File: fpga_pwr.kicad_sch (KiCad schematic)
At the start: 29 parts, among them Q1 BC817, U8 LFE5U-25F-8MG285C

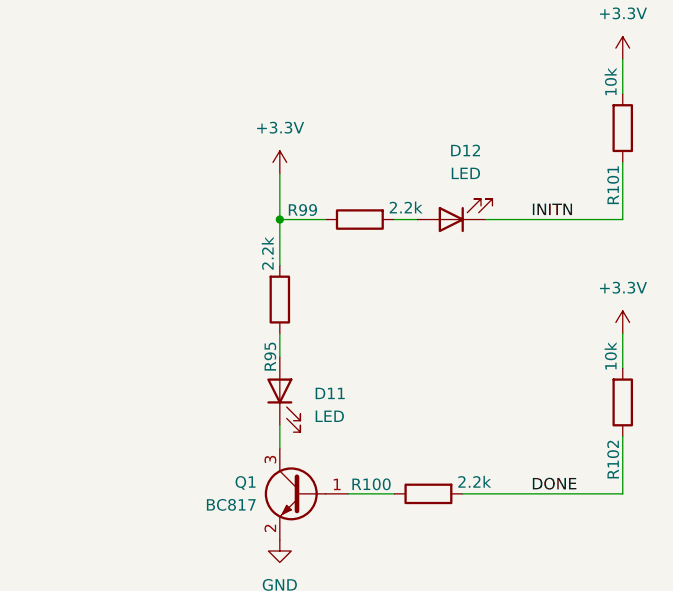
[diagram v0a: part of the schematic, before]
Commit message: Fix silkscreen. Add power led
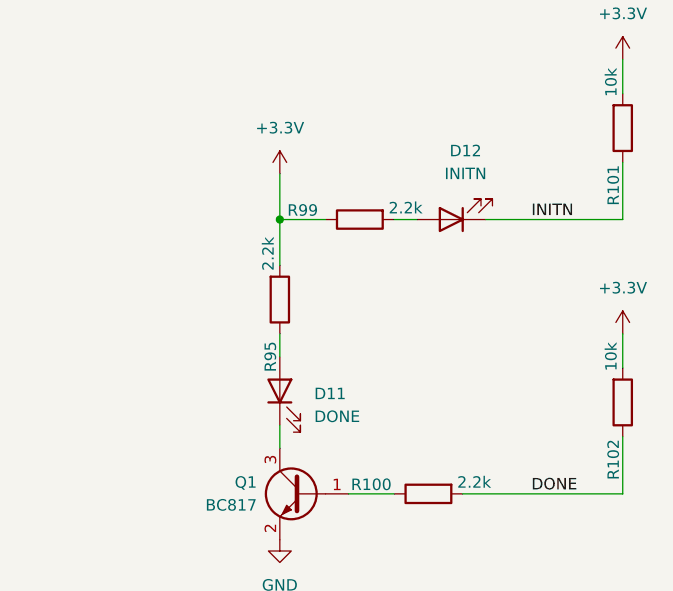
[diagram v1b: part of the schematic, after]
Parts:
- D11: value LED -> DONE
- D12: value LED -> INITN
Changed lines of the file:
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@@
 			)
 		)
-		(property "Value" "LED"
+		(property "Value" "INITN"
 			(at 236.5375 114.3 0)
 			(effects
@@
 			)
 		)
-		(property "Value" "LED"
+		(property "Value" "DONE"
 			(at 219.71 141.2874 90)
 			(effects
